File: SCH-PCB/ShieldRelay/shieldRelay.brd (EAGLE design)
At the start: 99 x 78.9 mm, 56 parts, among them IC1 LM2596SX-5.0_NOPB, K1 SLA-05VDC-SL-C, K2 SRD-05VDC-SL-C, K3 G3MB-202PL-DC5, K5 G3MB-202PL-DC5, K6 SRD-05VDC-SL-C, Q1 MMST2222A-7-F, Q2 MMST2222A-7-F, Q3 MMST2222A-7-F, Q4 MMST2222A-7-F, Q5 MMST2222A-7-F

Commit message: FEAT: update schematic
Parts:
- removed JP10: (no value), pinhead:2X04
- removed JP7: (no value), pinhead:1X03
- added GND, VIN: (no value), pinhead:2X04
- added JP13: (no value), pinhead_mod:1X15
- added VCC_SELECT: (no value), pinhead:1X03
- moved C17 2.30 mm to (91.2, 79.8)
- moved JP1 0.51 mm to (89.9, 50.8)
- moved JP5 0.51 mm to (95.0, 50.8)
- moved JP12 0.51 mm to (87.4, 50.8)
- moved JP4 0.51 mm to (92.5, 50.8)
- moved BOARD1 0.25 mm to (84.8, 33.0)
- renumbered JP8 to VCC, JP9 to GND_
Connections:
- net +3V3: now also VCC_SELECT.3; no longer JP7.3
- net +5V: now also VCC_SELECT.1; no longer JP7.1
- net GND: now also GND.1, GND.2, GND.3, GND.4, GND.5, GND.6, GND.7, GND.8
- net N$17: now also JP13.1
- net N$19: now also JP13.2
- net N$20: now also JP13.3
- net N$21: now also JP13.4
- net N$22: now also JP13.5
- net N$28: now also JP13.6
- net N$29: now also JP13.7
- net N$30: now also JP13.8
- net N$31: now also JP13.9
- net N$32: now also JP13.10
- net N$33: now also JP13.11
- net N$34: now also JP13.12
- net N$35: now also JP13.13
- net N$36: now also JP13.14
- net N$37: now also JP13.15
- net N$39: now also VCC_SELECT.2; no longer JP7.2
- net VCC/2: now also VIN.1, VIN.2, VIN.3, VIN.4, VIN.5, VIN.6, VIN.7, VIN.8; no longer JP10.1, JP10.2, JP10.3, JP10.4, JP10.5, JP10.6, JP10.7, JP10.8
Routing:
- net +5V: track 0.00 -> 172.2 mm, vias 0 -> 2
- net N$39: track 0.00 -> 158.3 mm
- net VCC/2: track 0.00 -> 65.9 mm, vias 0 -> 2
- net GND: track 0.00 -> 39.9 mm
- net N$14: track 0.00 -> 37.9 mm
- net N$5: track 0.00 -> 36.3 mm, vias 0 -> 1
- net N$11: track 0.00 -> 34.8 mm, vias 0 -> 1
- net N$18: track 0.00 -> 28.2 mm
- net N$3: track 0.00 -> 22.8 mm, vias 0 -> 1
- net IN1: track 0.00 -> 15.5 mm, vias 0 -> 1
- net IN2: track 0.00 -> 14.8 mm, vias 0 -> 1
- net IN3: track 0.00 -> 12.6 mm, vias 0 -> 1
- net VCC: track 0.00 -> 10.4 mm
- net N$8: track 0.00 -> 9.28 mm
- net IN4: track 0.00 -> 9.14 mm, vias 0 -> 1
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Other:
- board text added: "+"
- board text added: "-"
- board text added: "3V3"
- board text added: "5-30VDC"
- board text added: "5V"
- board text added: "ESP32-DEVKIT"
- board text added: "NODEMCU-AMICA"
- board text added: "NODEMCU-LOLIN"

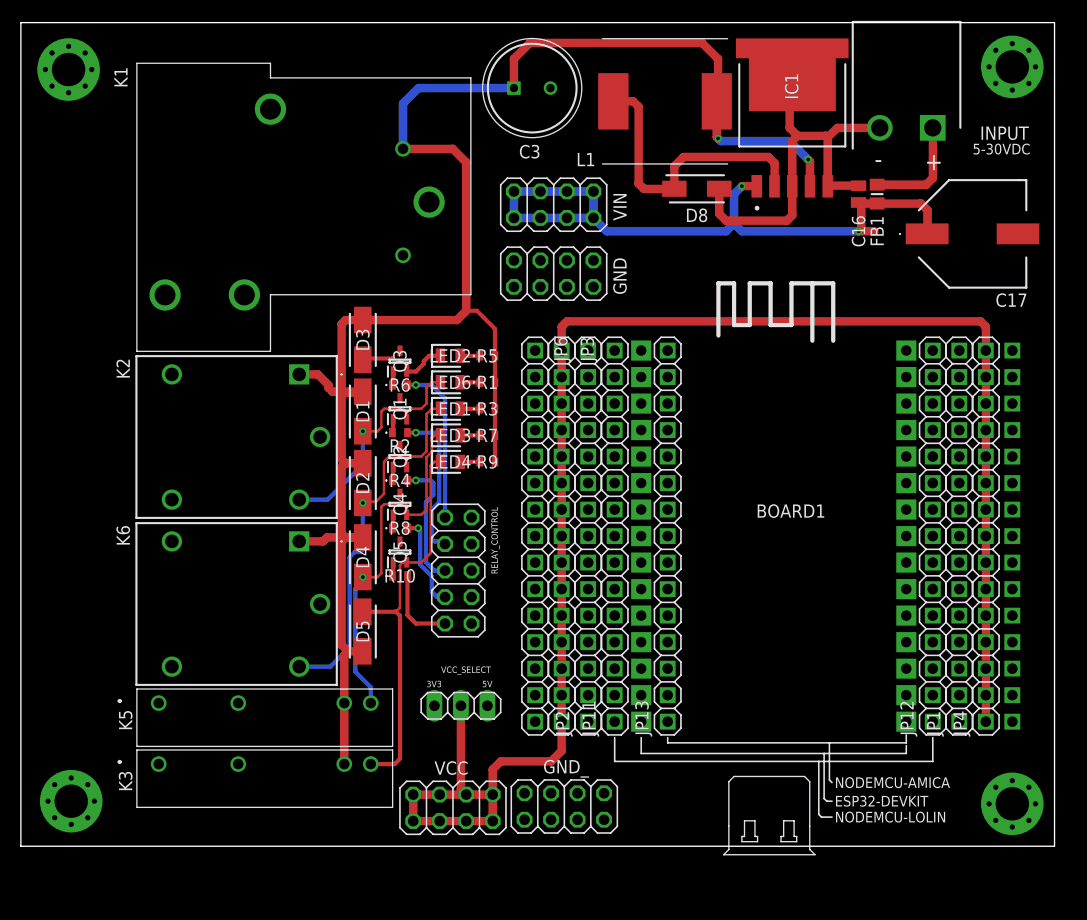
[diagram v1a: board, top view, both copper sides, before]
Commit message: FEAT: add 3v3 regulator
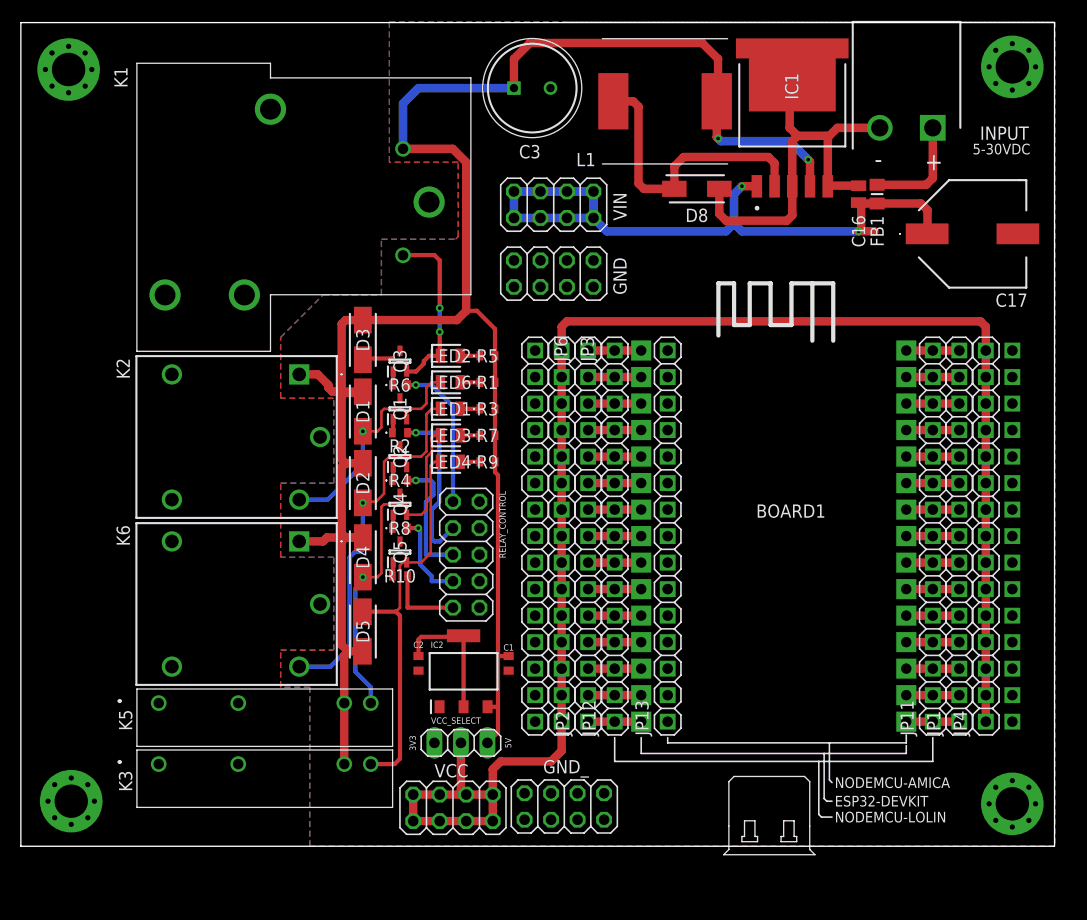
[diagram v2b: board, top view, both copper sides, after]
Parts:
- added C1, C2: 0.1uf, KGM15BR71E104KT:CAPC1608X95N
- added IC2: LM1117MPX-33NOPB, LM1117MPX-33NOPB:SOT230P700X180-4N
- C16: value KAF21KR71H225KU -> 2.2uf
- C17: value EEH-ZU1V681UP -> 680uf
- moved JP11 30.5 mm to (87.4, 50.8)
- moved JP12 30.5 mm to (56.9, 50.8)
- moved VCC_SELECT 3.56 mm to (42.2, 31.0)
- moved RELAY_CONTROL 1.70 mm to (42.7, 49.0)
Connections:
- removed net N$16: BOARD1.3V3
- removed net N$40: BOARD1.D15
- removed net N$41: BOARD1.D2
- removed net N$42: BOARD1.D4
- removed net N$43: BOARD1.D16
- removed net N$44: BOARD1.D17
- removed net N$45: BOARD1.D5
- removed net N$46: BOARD1.D18
- removed net N$47: BOARD1.D19
- removed net N$48: BOARD1.D21
- removed net N$49: BOARD1.D3
- removed net N$50: BOARD1.D1
- removed net N$51: BOARD1.D22
- removed net N$52: BOARD1.D23
- removed net N$53: BOARD1.EN
- removed net N$54: BOARD1.VP
- removed net N$55: BOARD1.VN
- removed net N$56: BOARD1.D34
- removed net N$57: BOARD1.D35
- removed net N$58: BOARD1.D32
- removed net N$59: BOARD1.D33
- removed net N$60: BOARD1.D25
- removed net N$61: BOARD1.D26
- removed net N$62: BOARD1.D27
- removed net N$63: BOARD1.D14
- removed net N$64: BOARD1.D12
- removed net N$65: BOARD1.D13
- removed net N$66: BOARD1.GND
- removed net N$67: BOARD1.VIN
- new net 1: BOARD1.3V3, JP1.1, JP11.1
- new net 10: BOARD1.D19, JP1.10, JP11.10
- new net 11: BOARD1.D21, JP1.11, JP11.11
- new net 12: BOARD1.D3, JP1.12, JP11.12
- new net 13: BOARD1.D1, JP1.13, JP11.13
- new net 14: BOARD1.D22, JP1.14, JP11.14
- new net 15: BOARD1.D23, JP1.15, JP11.15
- new net 16: BOARD1.VIN, JP12.1, JP2.1
- new net 17: BOARD1.GND, JP12.2, JP2.2
- new net 18: BOARD1.D13, JP12.3, JP2.3
- new net 19: BOARD1.D12, JP12.4, JP2.4
- new net 2: BOARD1.GND@1, JP1.2, JP11.2
- new net 20: BOARD1.D14, JP12.5, JP2.5
- new net 21: BOARD1.D27, JP12.6, JP2.6
- new net 22: BOARD1.D26, JP12.7, JP2.7
- new net 23: BOARD1.D25, JP12.8, JP2.8
- new net 24: BOARD1.D33, JP12.9, JP2.9
- new net 25: BOARD1.D32, JP12.10, JP2.10
- new net 26: BOARD1.D35, JP12.11, JP2.11
- new net 27: BOARD1.D34, JP12.12, JP2.12
- new net 28: BOARD1.VN, JP12.13, JP2.13
- new net 29: BOARD1.VP, JP12.14, JP2.14
- new net 3: BOARD1.D15, JP1.3, JP11.3
- new net 30: BOARD1.EN, JP12.15, JP2.15
- new net 4: BOARD1.D2, JP1.4, JP11.4
- new net 5: BOARD1.D4, JP1.5, JP11.5
- new net 6: BOARD1.D16, JP1.6, JP11.6
- new net 7: BOARD1.D17, JP1.7, JP11.7
- new net 8: BOARD1.D5, JP1.8, JP11.8
- new net 9: BOARD1.D18, JP1.9, JP11.9
- net +5V: now also C1.2, IC2.3
- net GND: now also C1.1, C2.1
- net N$17: no longer JP1.1, JP11.1, JP12.1, JP2.1
- net N$19: no longer JP1.2, JP11.2, JP12.2, JP2.2
- net N$20: no longer JP1.3, JP11.3, JP12.3, JP2.3
- net N$21: no longer JP1.4, JP11.4, JP12.4, JP2.4
- net N$22: no longer JP1.5, JP11.5, JP12.5, JP2.5
- net N$28: no longer JP1.6, JP11.6, JP12.6, JP2.6
- net N$29: no longer JP1.7, JP11.7, JP12.7, JP2.7
- net N$30: no longer JP1.8, JP11.8, JP12.8, JP2.8
- net N$31: no longer JP1.9, JP11.9, JP12.9, JP2.9
- net N$32: no longer JP1.10, JP11.10, JP12.10, JP2.10
- net N$33: no longer JP1.11, JP11.11, JP12.11, JP2.11
- net N$34: no longer JP1.12, JP11.12, JP12.12, JP2.12
- net N$35: no longer JP1.13, JP11.13, JP12.13, JP2.13
- net N$36: no longer JP1.14, JP11.14, JP12.14, JP2.14
- net N$37: no longer JP1.15, JP11.15, JP12.15, JP2.15
- net N$38: now also C2.2, IC2.2, IC2.4; no longer BOARD1.GND@1
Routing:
- net +5V: track 172.2 -> 201.7 mm
- net N$8: track 9.28 -> 22.2 mm, vias 0 -> 2
- net N$38: track 0.00 -> 12.8 mm
- net 30: track 0.00 -> 6.31 mm
- net 9: track 0.00 -> 5.08 mm
- net 8: track 0.00 -> 5.08 mm
- net 7: track 0.00 -> 5.08 mm
- net 6: track 0.00 -> 5.08 mm
- net 5: track 0.00 -> 5.08 mm
- net 4: track 0.00 -> 5.08 mm
- net 3: track 0.00 -> 5.08 mm
- net 29: track 0.00 -> 5.08 mm
- net 28: track 0.00 -> 5.08 mm
- net 27: track 0.00 -> 5.08 mm
- net 26: track 0.00 -> 5.08 mm
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- added copper zone on layer 1, net GND
- added copper zone on layer 16, net GND

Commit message: FEAT: update board
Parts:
- moved JP5 0.25 mm to (95.2, 50.8), flipped to the top
- moved K2 0.25 mm to (26.4, 66.3)
- moved K6 0.25 mm to (26.4, 50.3)
- moved K3 0.25 mm to (13.0, 29.0)
- moved K5 0.25 mm to (13.0, 34.8)
- renumbered BOARD1 to BOARD, GND to GND_1, GND_ to GND_2, LED1 to RL3, LED2 to RL1, LED3 to RL4, LED4 to RL5, LED6 to RL2
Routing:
- net +5V: track 201.7 -> 211.8 mm, vias 2 -> 7
- net VCC/2: track 65.9 -> 68.4 mm
- net N$3: track 22.8 -> 24.7 mm
- net N$5: track 36.3 -> 37.5 mm

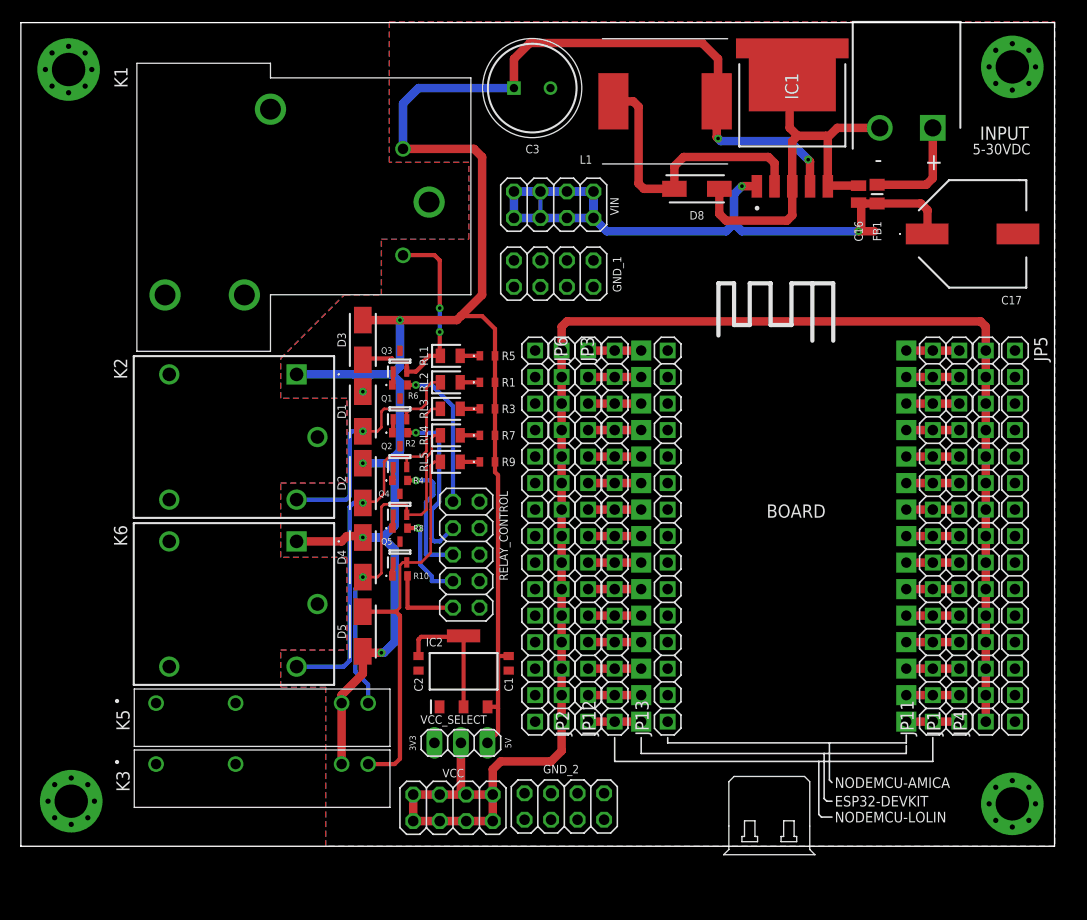
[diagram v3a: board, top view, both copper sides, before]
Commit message: FEAT: update terminal block
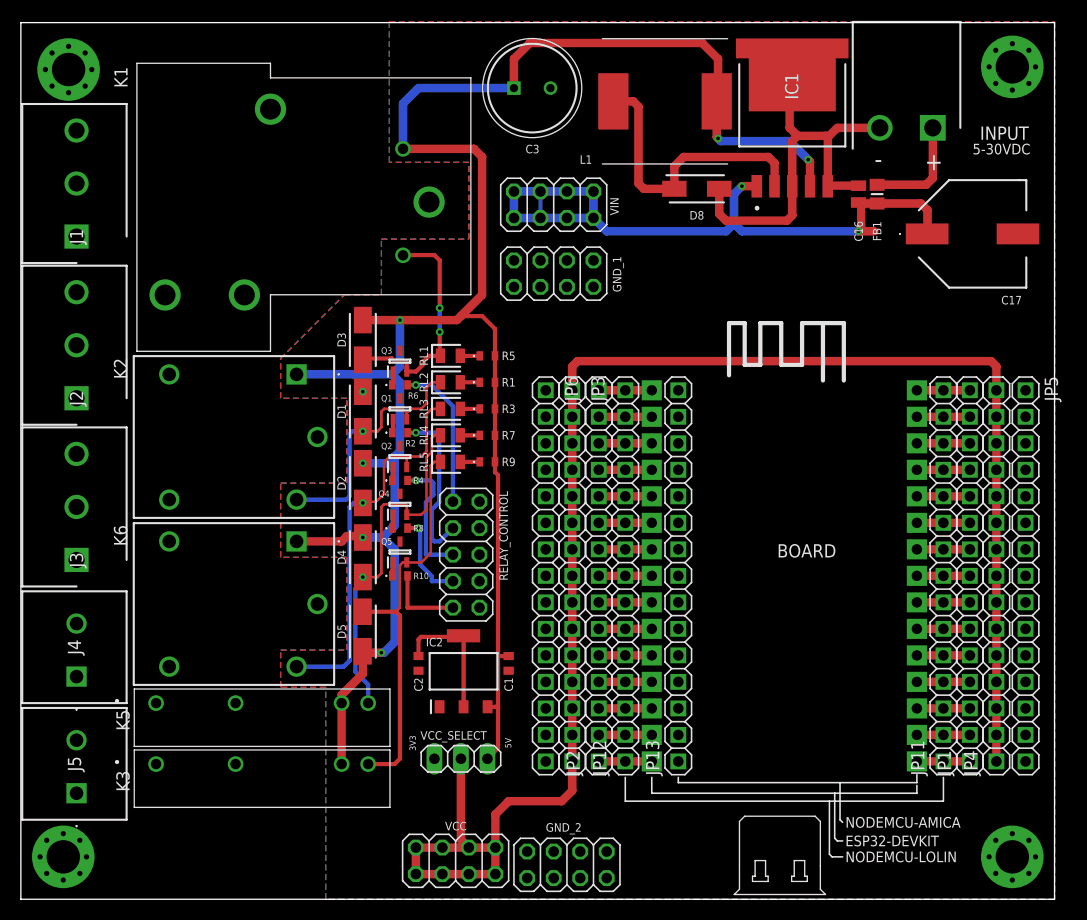
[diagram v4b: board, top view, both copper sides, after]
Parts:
- added J1, J2, J3: 1716090000, 1716090000:SHDR3W95P0X508_1X3_1524X1000X1
- added J4, J5: 1716080000, 1716080000:1716080000
- moved GND_2 5.59 mm to (52.3, 19.3)
- moved H4 5.39 mm to (4.06, 20.1)
- moved VCC 5.09 mm to (41.7, 19.7)
- moved H3 5.08 mm to (95.0, 20.1)
- moved BOARD 3.94 mm to (85.9, 29.2)
- moved JP1 3.94 mm to (90.9, 47.0)
- moved JP5 3.94 mm to (96.3, 47.0)
- moved JP12 3.94 mm to (57.9, 47.0)
- moved JP13 3.94 mm to (63.0, 47.0)
- moved JP2 3.94 mm to (55.4, 47.0)
- moved JP3 3.94 mm to (52.8, 47.0)
- moved JP6 3.94 mm to (50.3, 47.0)
- moved JP11 3.94 mm to (88.4, 47.0)
- moved JP4 3.94 mm to (93.5, 47.0)
- moved VCC_SELECT 1.52 mm to (42.2, 29.5)
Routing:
- net N$39: track 154.8 -> 160.2 mm
- net +5V: track 211.8 -> 213.3 mm
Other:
- board size 99 x 78.9 mm -> 99 x 84 mm

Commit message: DOC: UPDATE SCHEMATIC, BOARD AND ADD PDF
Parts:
- moved H1 0.57 mm to (4.06, 95.8)
- renumbered J1 to RELAY1, J2 to RELAY2, J3 to RELAY3, J4 to RELAY4, J5 to RELAY5, JP1 to SIGNAL_4, JP2 to SIGNAL_3, JP3 to VCC_3, JP4 to VCC_4, JP5 to GND_4, JP6 to GND_3
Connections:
- removed net 16: BOARD.VIN, JP12.1, SIGNAL_3.1
- removed net 17: BOARD.GND, JP12.2, SIGNAL_3.2
- removed net N$17: JP13.1
- removed net N$19: JP13.2
- removed net N$20: JP13.3
- removed net N$21: JP13.4
- removed net N$22: JP13.5
- removed net N$28: JP13.6
- removed net N$29: JP13.7
- removed net N$30: JP13.8
- removed net N$31: JP13.9
- removed net N$32: JP13.10
- removed net N$33: JP13.11
- removed net N$34: JP13.12
- removed net N$35: JP13.13
- removed net N$36: JP13.14
- removed net N$37: JP13.15
- new net COM1: K2.5, RELAY2.2
- new net COM2: K1.1, K1.2, RELAY1.2
- new net COM3: K6.5, RELAY3.2
- new net COM4: K3.1, RELAY5.1
- new net COM5: K5.1, RELAY4.1
- new net NC1: K2.3, RELAY2.1
- new net NC2: K1.4, RELAY1.1
- new net NC3: K6.3, RELAY3.1
- new net NO1: K2.2, RELAY2.3
- new net NO2: K1.3, RELAY1.3
- new net NO3: K6.2, RELAY3.3
- new net NO4: K3.2, RELAY5.2
- new net NO5: K5.2, RELAY4.2
- net +5V: now also BOARD.VIN, JP12.1, JP13.1, SIGNAL_3.1
- net 18: now also JP13.3
- net 19: now also JP13.4
- net 20: now also JP13.5
- net 21: now also JP13.6
- net 22: now also JP13.7
- net 23: now also JP13.8
- net 24: now also JP13.9
- net 25: now also JP13.10
- net 26: now also JP13.11
- net 27: now also JP13.12
- net 28: now also JP13.13
- net 29: now also JP13.14
- net 30: now also JP13.15
- net GND: now also BOARD.GND, JP12.2, JP13.2, SIGNAL_3.2
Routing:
- net +5V: track 213.3 -> 312.8 mm, vias 7 -> 8
- net NO2: track 0.00 -> 60.9 mm
- net COM2: track 0.00 -> 45.6 mm
- net COM3: track 0.00 -> 26.9 mm
- net COM1: track 0.00 -> 26.7 mm
- net NO5: track 0.00 -> 25.3 mm
- net NO4: track 0.00 -> 17.3 mm
- net NC3: track 0.00 -> 13.9 mm
- net NC1: track 0.00 -> 13.4 mm
- net NC2: track 0.00 -> 13.0 mm
- net NO1: track 0.00 -> 12.9 mm
- net NO3: track 0.00 -> 12.4 mm
- net COM5: track 0.00 -> 9.71 mm
- net COM4: track 0.00 -> 9.37 mm
- net GND: track 39.9 -> 47.6 mm, vias 0 -> 24
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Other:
- board size 99 x 84 mm -> 99.1 x 84.1 mm
- board text added: "COM"
- board text added: "DESIGN BY POSITRON ELEKTRONIK"
- board text added: "ESP32/NODEMCU RELAY SHIELD"
- board text added: "NC"
- board text added: "NO"

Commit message: FEAT: add 3D model
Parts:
- moved D3 14.3 mm to (47.0, 71.4), turned to 0 degrees
- moved K1 0.24 mm to (39.1, 83.0), flipped to the bottom, turned to 270 degrees
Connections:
- net +5V: now also K1.6; no longer K1.5
- net N$8: now also K1.5; no longer K1.6
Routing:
- net NO2: track 60.9 -> 27.6 mm
- net +5V: track 312.8 -> 302.4 mm
- net NC2: track 13.0 -> 20.1 mm
- net COM2: track 45.6 -> 52.4 mm
- net N$8: track 22.2 -> 28.0 mm, vias 2 -> 3

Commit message: FEAT: add gerber file
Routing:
- net COM2: track 52.4 -> 43.5 mm
- net NO1: track 12.9 -> 15.7 mm
- net COM1: track 26.7 -> 29.4 mm
- net NO2: track 27.6 -> 25.8 mm
- net N$5: track 37.5 -> 38.4 mm
- net N$11: track 34.7 -> 34.1 mm
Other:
- outline, holes or cut-outs redrawn
